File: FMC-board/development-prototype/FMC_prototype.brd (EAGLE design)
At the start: 103.8 x 69.8 mm, 65 parts, among them J1 DC_POWER_JACK-PJ-102AH, J2 DC_POWER_JACK-PJ-102AH

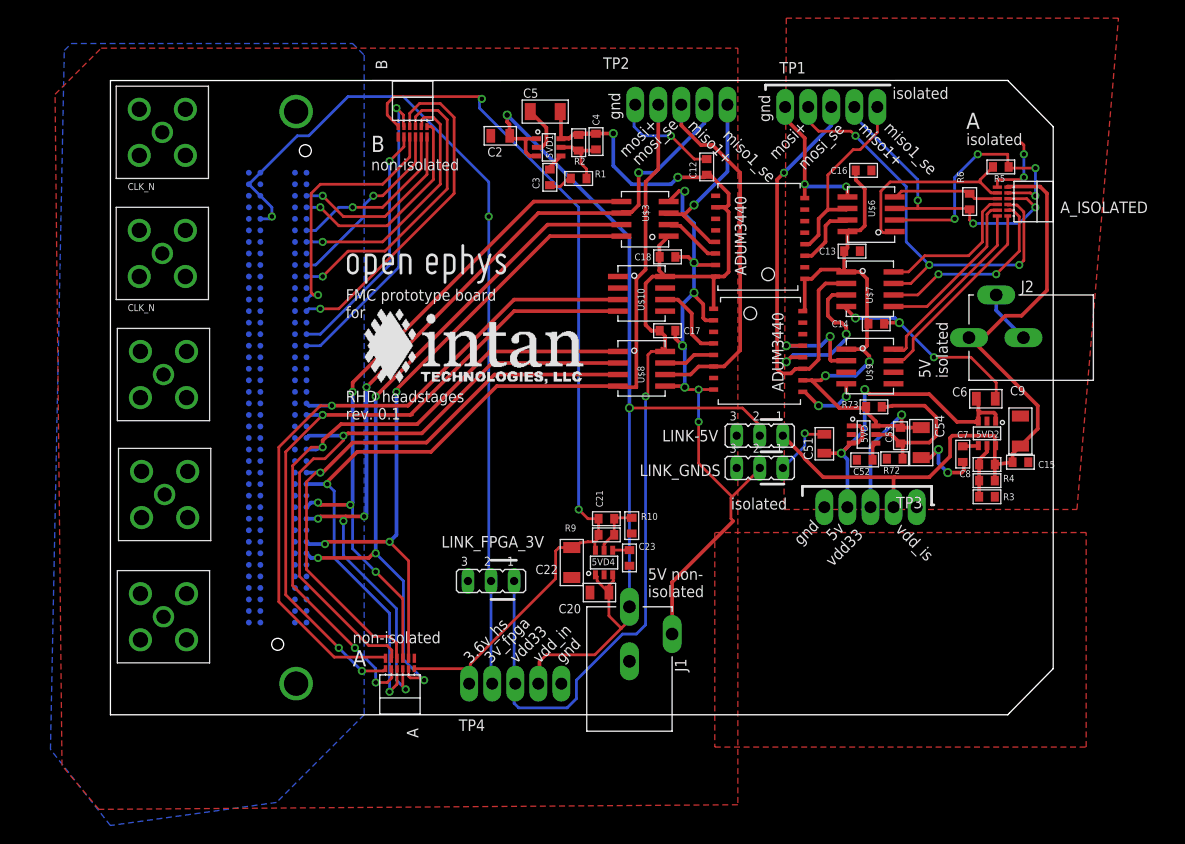
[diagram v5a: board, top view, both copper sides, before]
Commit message: added measurement points (just+) to all B connector LVDS signals
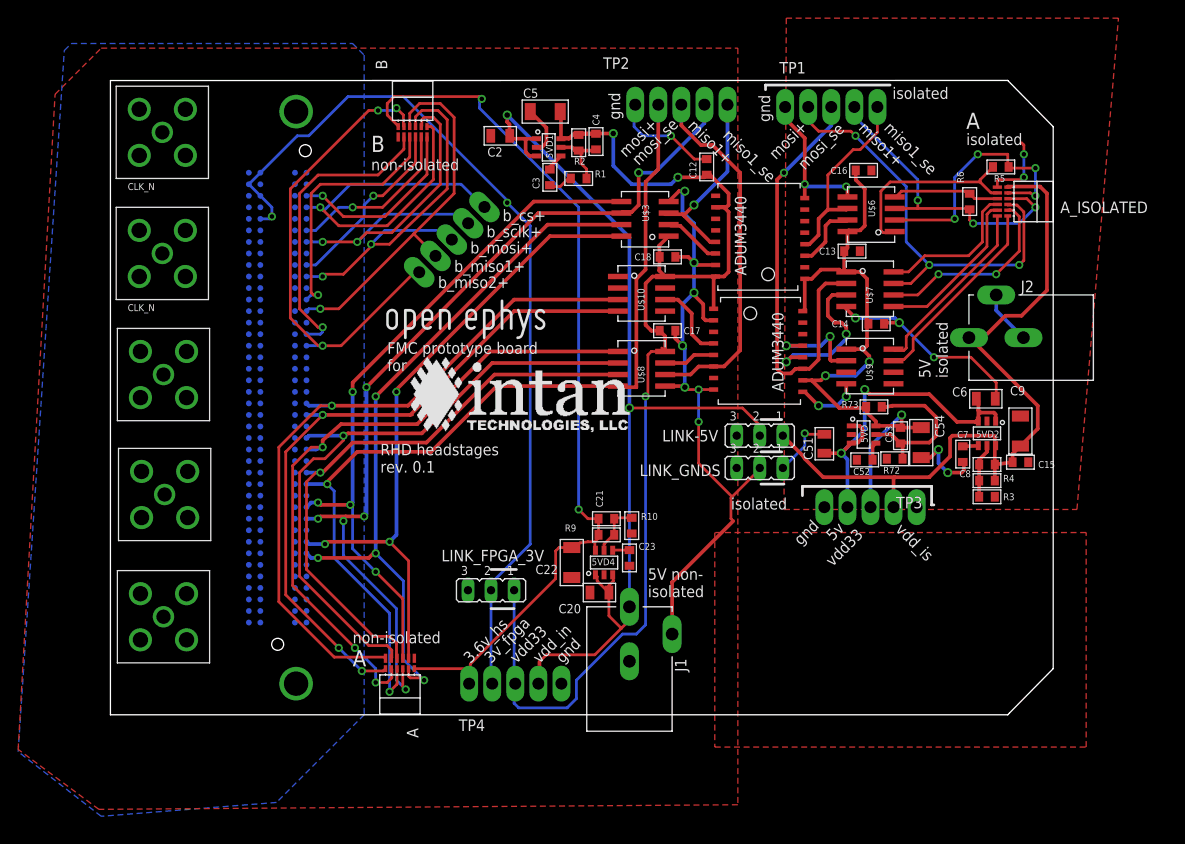
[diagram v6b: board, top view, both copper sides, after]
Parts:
- added TP5: TP5P5-25-13, testpad:P5-25-13
- moved U$1 7.47 mm to (29.7, 40.9)
- moved U$16 7.37 mm to (32.5, 30.5)
- moved LINK_FPGA_3V 1.02 mm to (41.9, 13.7)
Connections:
- net B_CS+: now also TP5.TP-5
- net B_MISO1+: now also TP5.TP-2
- net B_MISO2+: now also TP5.TP-1
- net B_MOSI+: now also TP5.TP-3
- net B_SCLK+: now also TP5.TP-4
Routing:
- net B_CS+: track 23.3 -> 43.8 mm
- net B_MISO2+: track 33.7 -> 53.1 mm, vias 1 -> 3
- net B_SCLK+: track 27.2 -> 41.1 mm, vias 1 -> 2
- net B_MOSI+: track 32.4 -> 42.4 mm, vias 1 -> 2
- net B_MISO2-: track 27.1 -> 33.3 mm
- net B_MISO1+: track 37.4 -> 40.9 mm
- net 3V_FPGA: track 96.2 -> 99.6 mm
- net VDD33: track 135.1 -> 134.1 mm
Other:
- board text added: "b_cs+"
- board text added: "b_miso1+"
- board text added: "b_miso2+"
- board text added: "b_mosi+"
- board text added: "b_sclk+"

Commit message: added proper ground plane
this is now 4 layers but its somewhat cleaner  this way
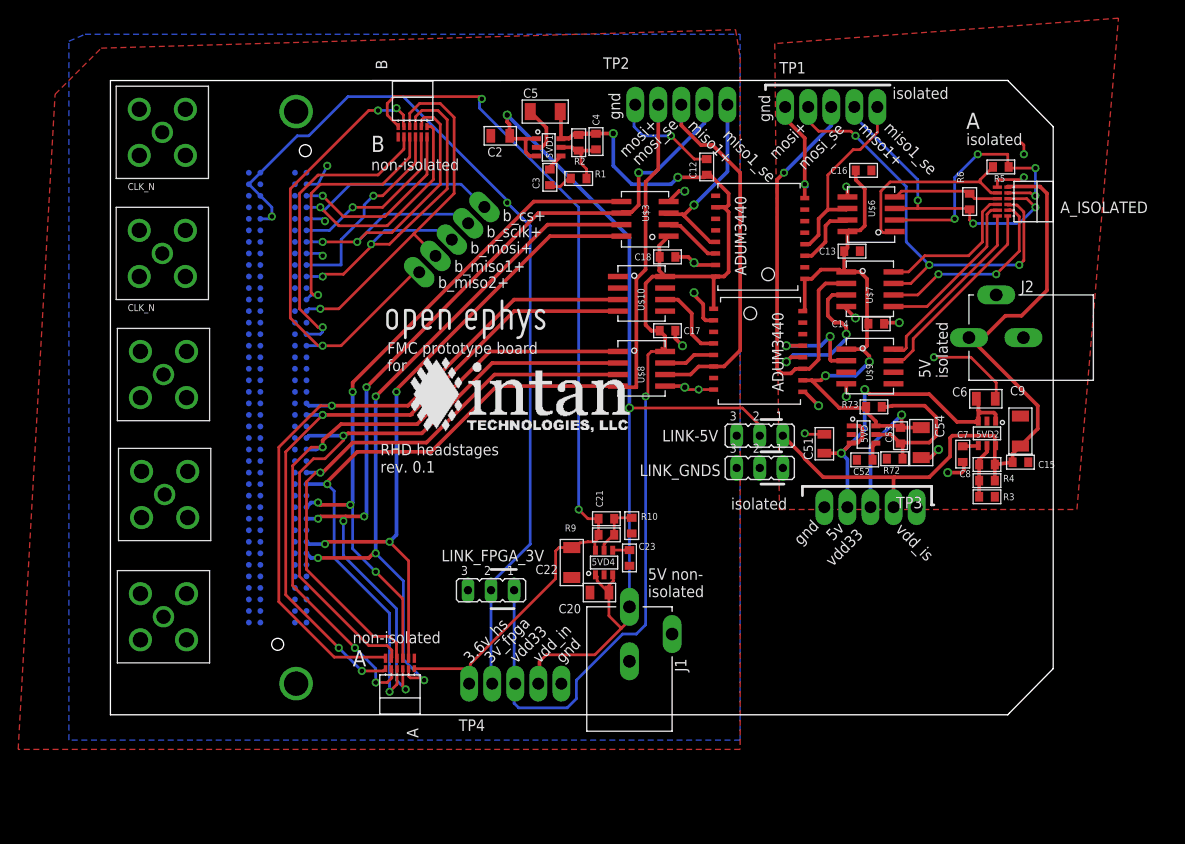
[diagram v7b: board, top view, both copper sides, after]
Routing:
- net GND_ISOLATED: track 77.2 -> 42.0 mm
- net GND: track 97.8 -> 69.5 mm, vias 8 -> 10
- net B_MOSI-: track 20.3 -> 21.9 mm
- added copper zone on layer 2, net GND
- added copper zone on layer 2, net GND_ISOLATED

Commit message: added testpoints
still some unrouted parts
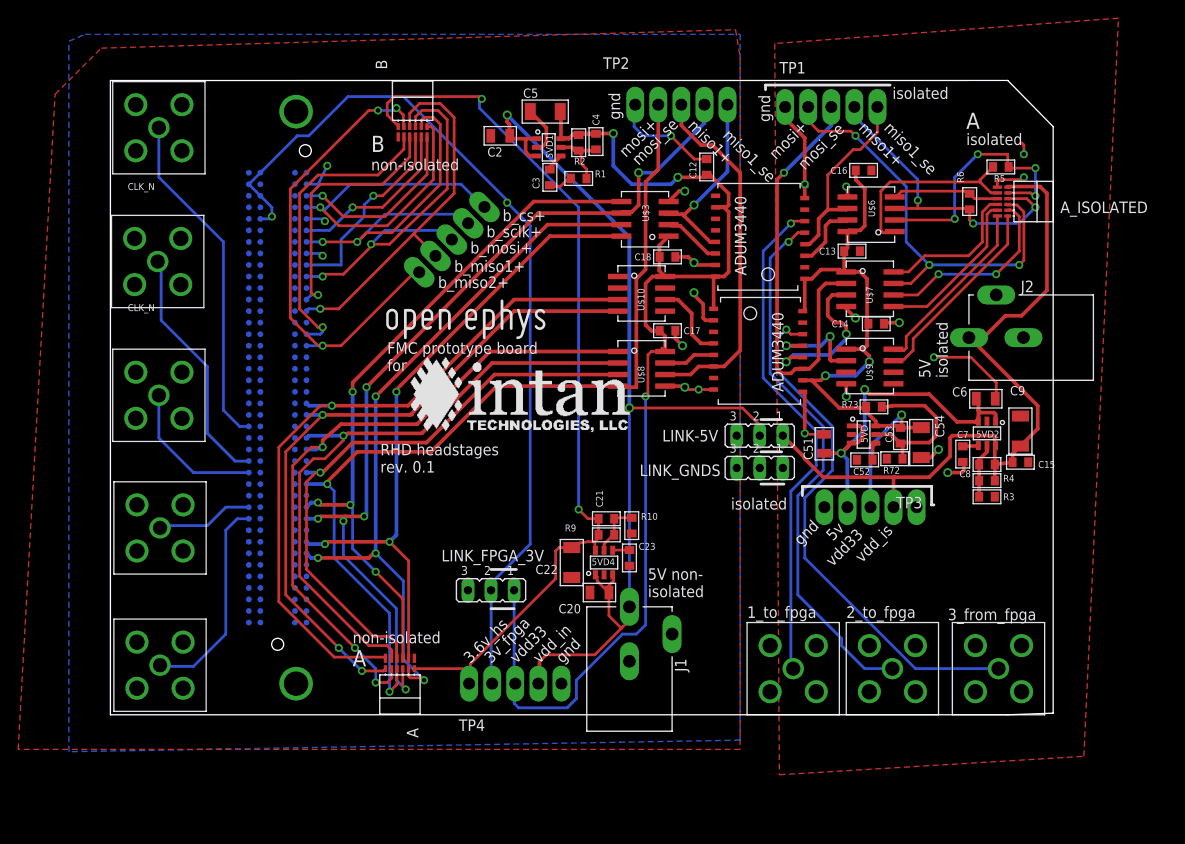
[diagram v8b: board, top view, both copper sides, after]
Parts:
- added U$17, U$18, U$19: SMA_JACK_142-0701-201_DEV, SA_BB:SMA_JACK_142-0701-201
- moved U$5 58.7 mm to (5.46, 5.46)
- moved U$2 30.2 mm to (5.46, 20.6)
- moved U$15 27.2 mm to (5.33, 64.6)
- moved U$14 25.7 mm to (5.21, 49.9)
- moved U$13 24.4 mm to (5.33, 35.2)
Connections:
- new net TP1_FROM_SMA: U$11.P5, U$19.CLK
- new net TP1_TO_FPGA: U$11.P12, U$4.P$22
- new net TP2_FROM_SMA: U$11.P6, U$17.CLK
- new net TP2_TO_FPGA: U$11.P11, U$4.P$23
- new net TP3_FROM_FPGA: U$12.P3, U$4.P$62
- new net TP3_TO_SMA: U$12.P14, U$18.CLK
- new net TP4: U$4.P$130, U$5.CLK
- new net TP5: U$2.CLK, U$4.P$131
- new net TP6: U$13.CLK, U$4.P$134
- new net TP7: U$14.CLK, U$4.P$135
- new net TP8: U$15.CLK, U$4.P$138
- net GND_ISOLATED: now also U$17.GND$1, U$17.GND$2, U$17.GND$3, U$17.GND$4, U$18.GND$1, U$18.GND$2, U$18.GND$3, U$18.GND$4, U$19.GND$1, U$19.GND$2, U$19.GND$3, U$19.GND$4
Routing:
- net TP1_FROM_SMA: track 0.00 -> 60.2 mm, vias 0 -> 1
- net TP3_TO_SMA: track 0.00 -> 57.8 mm, vias 0 -> 1
- net TP2_FROM_SMA: track 0.00 -> 55.6 mm, vias 0 -> 1
- net TP8: track 0.00 -> 37.6 mm
- net TP7: track 0.00 -> 27.0 mm
- net GND: track 69.5 -> 94.2 mm
- net TP4: track 0.00 -> 23.3 mm
- net TP6: track 0.00 -> 16.2 mm
- net TP5: track 0.00 -> 10.7 mm
- net GND_ISOLATED: track 42.0 -> 44.7 mm, vias 12 -> 11
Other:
- outline, holes or cut-outs redrawn
- board text added: "1_to_fpga"
- board text added: "2_to_fpga"
- board text added: "3_from_fpga"
